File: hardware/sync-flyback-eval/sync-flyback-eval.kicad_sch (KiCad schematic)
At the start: 95 parts, among them J1 RJ45_LED_Shielded, Q1 SiR422DP, Q2 Si7898DP, Q3 MMDT3906, T1 PoE_Transformer, T2 Pulse_Transformer, U1 TPS23754PWPR, U2 TCMT1107

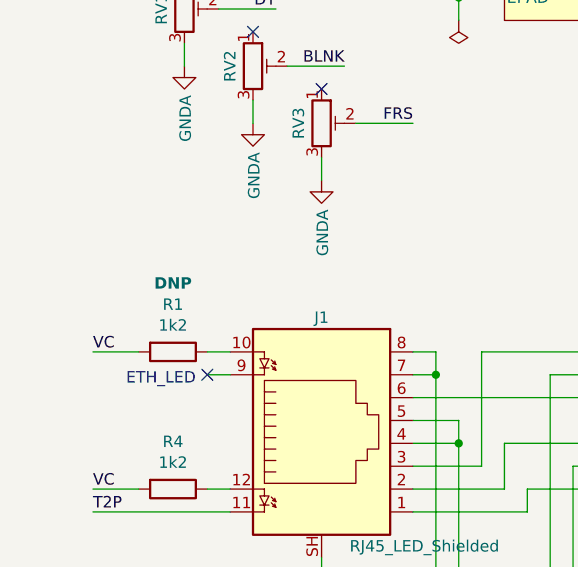
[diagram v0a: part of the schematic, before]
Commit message: flyback: place the current-limiting resistor for the jack
I didn't think I had this spec'd or sourced already.
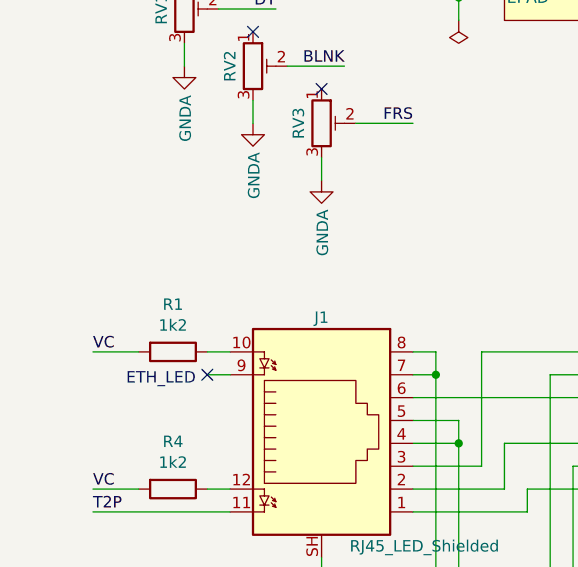
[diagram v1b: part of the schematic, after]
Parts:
- R1: Placement DNP -> (none)
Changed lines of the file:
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@@
       (effects (font (size 1.27 1.27)) hide)
-    )
-    (property "Placement" "DNP" (id 4) (at 29.21 106.68 90)
-      (effects (font (size 1.27 1.27) bold))
     )
     (pin "1")

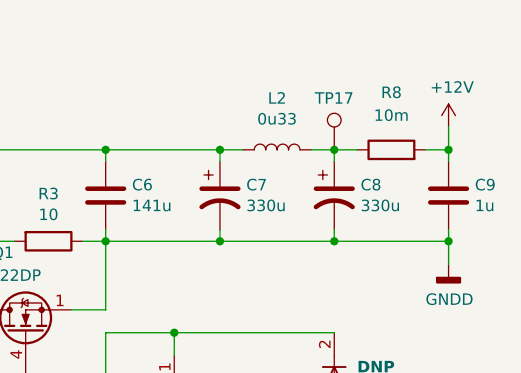
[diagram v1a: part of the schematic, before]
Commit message: flyback: improve testpoints
This changes a number of footprints to be through-hole instead of a
pad. The current sense resistor on the output was also moved to the
outside of the secondary-side output coupling capacitor; plus, an
extra testpoint was added to the other side.
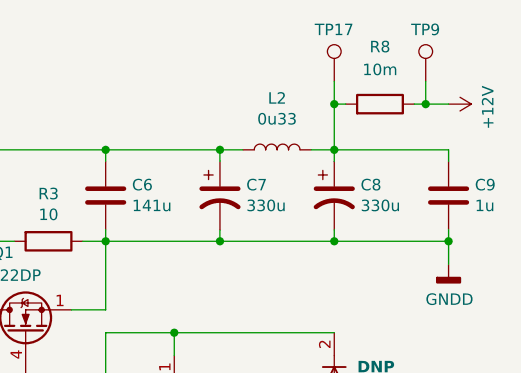
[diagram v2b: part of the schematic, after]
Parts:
- added TP9: VB, TestPoint:TestPoint_Loop_D1.80mm_Drill1.0mm_Beaded, symbol Connector:TestPoint
- TP10, TP11, TP13, TP14, TP15, TP16, TP17, TP2, TP7: footprint TestPoint:TestPoint_Pad_1.5x1.5mm -> TestPoint:TestPoint_Loop_D1.80mm_Drill1.0mm_Beaded
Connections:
- net +12V: now also R8.1, TP9.1; no longer C9.1, R8.2
- net at C8.1, L2.2, TP17.1: now also C9.1, R8.2; no longer R8.1
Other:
- moved on the sheet: R8, TP17

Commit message: flyback: customize a few footprints
These new ones have 3D models.
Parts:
- L1, L2: footprint Inductor_SMD:L_Abracon_ASPI-0630LR -> common:L_Abracon_ASPI-0630LR
- Q1, Q2: footprint Package_SO:PowerPAK_SO-8_Single -> common:PowerPAK_SO-8_Single
- TR1: footprint Transformer_SMD:Transformer_Ethernet_Bourns_PT61017PEL -> common:PT61017PEL
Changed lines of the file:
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@@
     (property "Reference" "L1" (id 0) (at 118.11 18.415 90))
     (property "Value" "3u3" (id 1) (at 118.11 20.7264 90))
-    (property "Footprint" "Inductor_SMD:L_Abracon_ASPI-0630LR" (id 2) (at 118.11 24.13 0)
+    (property "Footprint" "common:L_Abracon_ASPI-0630LR" (id 2) (at 118.11 24.13 0)
       (effects (font (size 1.27 1.27)) hide)
     )
@@
     (property "Reference" "L2" (id 0) (at 242.57 23.495 90))
     (property "Value" "0u33" (id 1) (at 242.57 25.8064 90))
-    (property "Footprint" "Inductor_SMD:L_Abracon_ASPI-0630LR" (id 2) (at 242.57 29.21 0)
+    (property "Footprint" "common:L_Abracon_ASPI-0630LR" (id 2) (at 242.57 29.21 0)
       (effects (font (size 1.27 1.27)) hide)
     )
@@
     (property "Reference" "TR1" (id 0) (at 88.9 135.6868 0))
     (property "Value" "PT61017PEL" (id 1) (at 88.9 133.3754 0))
-    (property "Footprint" "Transformer_SMD:Transformer_Ethernet_Bourns_PT61017PEL" (id 2) (at 88.9 109.22 0)
+    (property "Footprint" "common:PT61017PEL" (id 2) (at 88.9 109.22 0)
       (effects (font (size 1.27 1.27)) hide)
     )
@@
       (effects (font (size 1.27 1.27)) (justify left))
     )
-    (property "Footprint" "Package_SO:PowerPAK_SO-8_Single" (id 2) (at 171.45 66.675 0)
+    (property "Footprint" "common:PowerPAK_SO-8_Single" (id 2) (at 171.45 66.675 0)
       (effects (font (size 1.27 1.27) italic) (justify left) hide)
     )
@@
     (property "Reference" "Q1" (id 0) (at 212.09 40.64 90))
     (property "Value" "SiR422DP" (id 1) (at 212.09 43.18 90))
-    (property "Footprint" "Package_SO:PowerPAK_SO-8_Single" (id 2) (at 216.535 43.18 0)
+    (property "Footprint" "common:PowerPAK_SO-8_Single" (id 2) (at 216.535 43.18 0)
       (effects (font (size 1.27 1.27) italic) (justify left) hide)
     )
@@
     )
     (path "/00000000-0000-0000-0000-00005c1b084a"
-      (reference "L1") (unit 1) (value "3u3") (footprint "Inductor_SMD:L_Abracon_ASPI-0630LR")
+      (reference "L1") (unit 1) (value "3u3") (footprint "common:L_Abracon_ASPI-0630LR")
     )
     (path "/00000000-0000-0000-0000-00005d269ada"
-      (reference "L2") (unit 1) (value "0u33") (footprint "Inductor_SMD:L_Abracon_ASPI-0630LR")
+      (reference "L2") (unit 1) (value "0u33") (footprint "common:L_Abracon_ASPI-0630LR")
     )
     (path "/00000000-0000-0000-0000-00005ef82e6c"
-      (reference "Q1") (unit 1) (value "SiR422DP") (footprint "Package_SO:PowerPAK_SO-8_Single")
+      (reference "Q1") (unit 1) (value "SiR422DP") (footprint "common:PowerPAK_SO-8_Single")
     )
     (path "/00000000-0000-0000-0000-00005ef80cb3"
-      (reference "Q2") (unit 1) (value "Si7898DP") (footprint "Package_SO:PowerPAK_SO-8_Single")
+      (reference "Q2") (unit 1) (value "Si7898DP") (footprint "common:PowerPAK_SO-8_Single")
     )
     (path "/00000000-0000-0000-0000-00005d08d06f"
@@
     )
     (path "/00000000-0000-0000-0000-00005d6ac6f9"
-      (reference "TR1") (unit 1) (value "PT61017PEL") (footprint "Transformer_SMD:Transformer_Ethernet_Bourns_PT61017PEL")
+      (reference "TR1") (unit 1) (value "PT61017PEL") (footprint "common:PT61017PEL")
     )
     (path "/00000000-0000-0000-0000-00005d69703c"

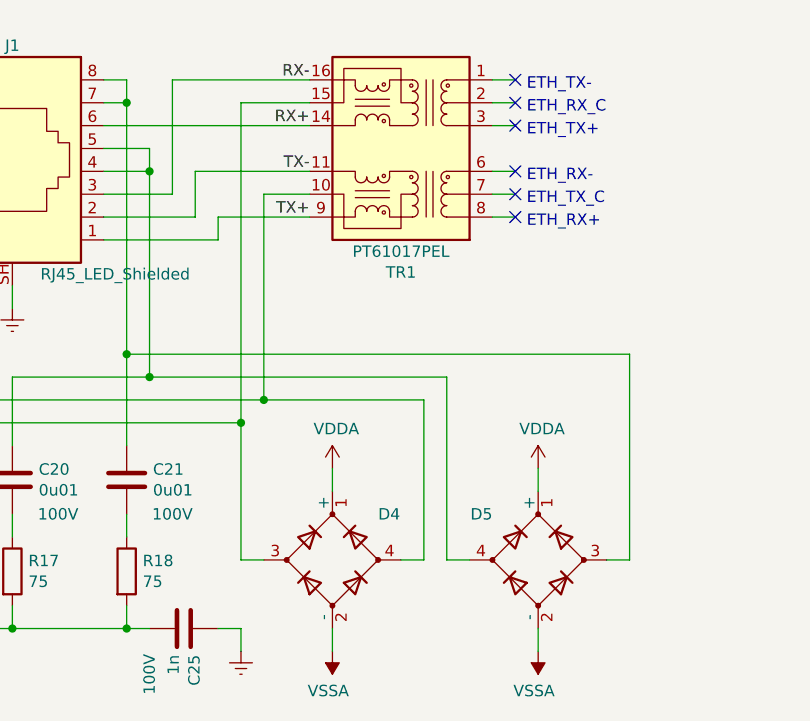
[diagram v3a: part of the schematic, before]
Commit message: flyback: shuffle a few connections to make layout easier
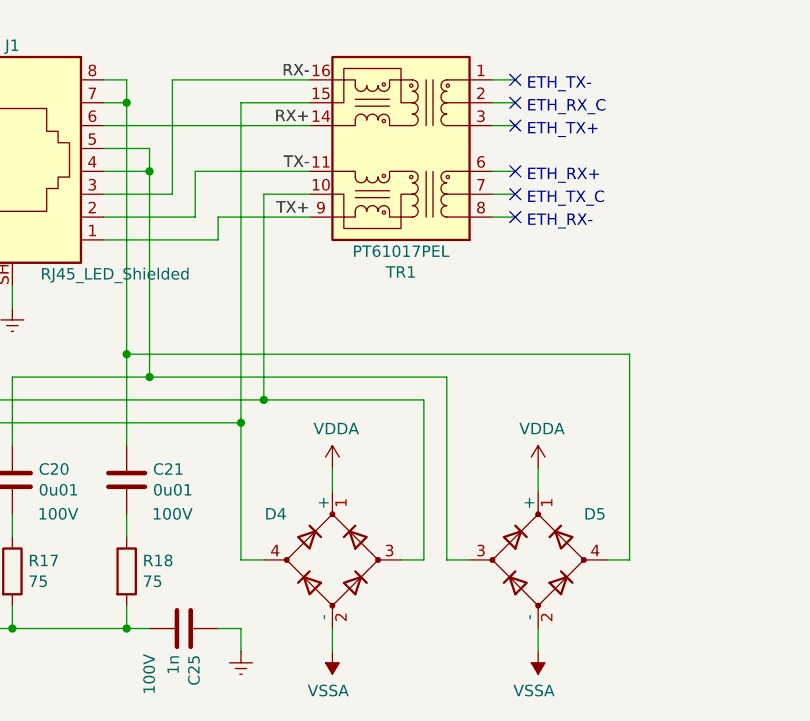
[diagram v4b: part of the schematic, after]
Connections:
- net at C20.1, J1.4, J1.5: now also D5.3; no longer D5.4
- net at C21.1, J1.7, J1.8: now also D5.4; no longer D5.3
- net at C18.1, TR1.15 (C_TX): now also D4.4; no longer D4.3
- net at C19.1, TR1.10 (C_RX): now also D4.3; no longer D4.4
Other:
- moved on the sheet: D4, D5
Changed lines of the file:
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@@
-    (stroke (width 0) (type default) (color 0 0 0 0))
-  )
-  (wire (pts (xy 68.58 132.08) (xy 68.58 129.54))
     (stroke (width 0) (type default) (color 0 0 0 0))
   )
@@
     (stroke (width 0) (type default) (color 0 0 0 0))
   )
-  (wire (pts (xy 66.04 124.46) (xy 78.74 124.46))
-    (stroke (width 0) (type default) (color 0 0 0 0))
-  )
   (wire (pts (xy 177.8 72.39) (xy 180.34 72.39))
     (stroke (width 0) (type default) (color 0 0 0 0))
@@
     (stroke (width 0) (type default) (color 0 0 0 0))
   )
+  (wire (pts (xy 68.58 129.54) (xy 78.74 129.54))
+    (stroke (width 0) (type default) (color 0 0 0 0))
+  )
   (wire (pts (xy 154.94 24.13) (xy 177.8 24.13))
     (stroke (width 0) (type default) (color 0 0 0 0))
@@
     (stroke (width 0) (type default) (color 0 0 0 0))
   )
+  (wire (pts (xy 55.88 129.54) (xy 66.04 129.54))
+    (stroke (width 0) (type default) (color 0 0 0 0))
+  )
   (wire (pts (xy 215.9 72.39) (xy 215.9 73.66))
     (stroke (width 0) (type default) (color 0 0 0 0))
@@
   )
   (wire (pts (xy 165.1 36.83) (xy 167.64 36.83))
-    (stroke (width 0) (type default) (color 0 0 0 0))
-  )
-  (wire (pts (xy 68.58 129.54) (xy 78.74 129.54))
     (stroke (width 0) (type default) (color 0 0 0 0))
   )
@@
     (stroke (width 0) (type default) (color 0 0 0 0))
   )
-  (wire (pts (xy 55.88 129.54) (xy 66.04 129.54))
+  (wire (pts (xy 66.04 124.46) (xy 78.74 124.46))
     (stroke (width 0) (type default) (color 0 0 0 0))
   )
@@
     (stroke (width 0) (type default) (color 0 0 0 0))
   )
+  (wire (pts (xy 68.58 132.08) (xy 68.58 129.54))
+    (stroke (width 0) (type default) (color 0 0 0 0))
+  )
   (wire (pts (xy 93.98 49.53) (xy 109.22 49.53))
     (stroke (width 0) (type default) (color 0 0 0 0))
@@
     (stroke (width 0) (type default) (color 0 0 0 0))
   )
-  (wire (pts (xy 66.04 129.54) (xy 66.04 124.46))
-    (stroke (width 0) (type default) (color 0 0 0 0))
-  )
   (wire (pts (xy 58.42 114.3) (xy 55.88 114.3))
     (stroke (width 0) (type default) (color 0 0 0 0))
@@
   )
   (wire (pts (xy 238.76 29.21) (xy 236.22 29.21))
+    (stroke (width 0) (type default) (color 0 0 0 0))
+  )
+  (wire (pts (xy 66.04 124.46) (xy 66.04 129.54))
     (stroke (width 0) (type default) (color 0 0 0 0))
   )
@@
     (effects (font (size 1.27 1.27)) (justify left bottom))
   )
-  (text "ETH_RX-" (at 102.87 125.73 0)
-    (effects (font (size 1.27 1.27)) (justify left bottom))
-  )
-  (text "ETH_RX+" (at 102.87 130.81 0)
+  (text "ETH_RX-" (at 102.87 130.81 0)
+    (effects (font (size 1.27 1.27)) (justify left bottom))
+  )
+  (text "ETH_RX+" (at 102.87 125.73 0)
     (effects (font (size 1.27 1.27)) (justify left bottom))
   )
@@
     (pin "2")
   )
-  (symbol (lib_id "Device:D_Bridge_+-AA") (at 81.28 167.64 90) (unit 1)
-    (in_bom yes) (on_board yes)
-    (property "Reference" "D4" (id 0) (at 86.36 162.56 90)
+  (symbol (lib_id "Device:D_Bridge_+-AA") (at 81.28 167.64 270) (mirror x) (unit 1)
+    (in_bom yes) (on_board yes)
+    (property "Reference" "D4" (id 0) (at 76.2 162.56 90)
       (effects (font (size 1.27 1.27)) (justify right))
     )
-    (property "Value" "D_Bridge_+-AA" (id 1) (at 89.9414 168.783 90)
+    (property "Value" "D_Bridge_+-AA" (id 1) (at 72.6186 168.783 90)
       (effects (font (size 1.27 1.27)) (justify right) hide)
     )
@@
     (pin "4")
   )
-  (symbol (lib_id "Device:D_Bridge_+-AA") (at 104.14 167.64 270) (mirror x) (unit 1)
-    (in_bom yes) (on_board yes)
-    (property "Reference" "D5" (id 0) (at 99.06 162.56 90)
+  (symbol (lib_id "Device:D_Bridge_+-AA") (at 104.14 167.64 90) (unit 1)
+    (in_bom yes) (on_board yes)
+    (property "Reference" "D5" (id 0) (at 109.22 162.56 90)
       (effects (font (size 1.27 1.27)) (justify right))
     )
-    (property "Value" "D_Bridge_+-AA" (id 1) (at 95.4786 168.783 90)
+    (property "Value" "D_Bridge_+-AA" (id 1) (at 112.8014 168.783 90)
       (effects (font (size 1.27 1.27)) (justify right) hide)
     )

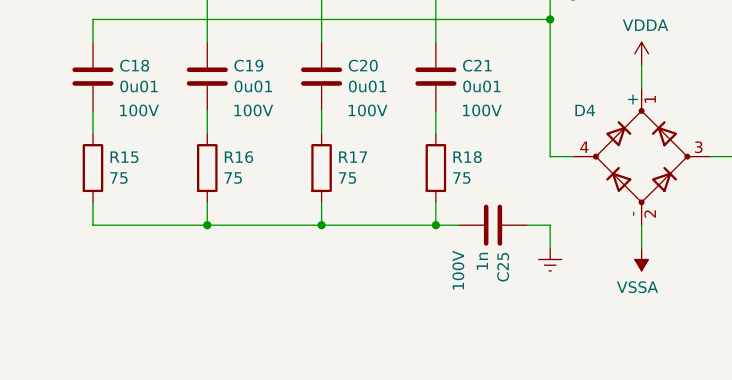
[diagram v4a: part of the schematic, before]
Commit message: flyback: add second earth-coupling capacitor to simplify pcb layout
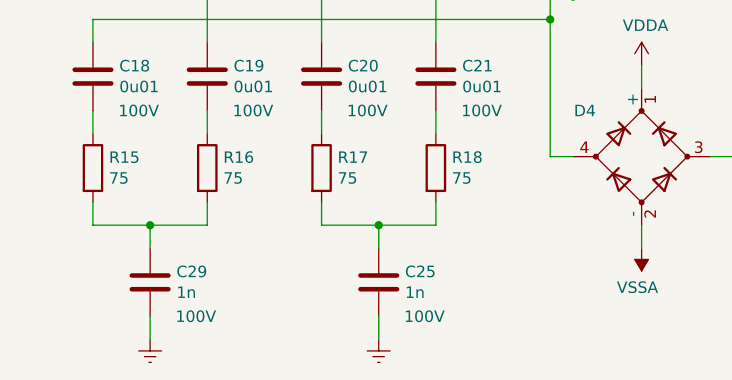
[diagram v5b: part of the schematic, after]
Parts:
- added C29: 1n, Capacitor_SMD:C_0402_1005Metric, symbol Device:C
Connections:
- net Earth: now also C25.2, C29.2; no longer C25.1
- new net: C29.1, R15.2, R16.2
- new net: C25.1, R17.2, R18.2
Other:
- moved on the sheet: C25
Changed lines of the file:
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@@
   (junction (at 111.76 24.13) (diameter 0) (color 0 0 0 0)
   )
-  (junction (at 58.42 175.26) (diameter 0) (color 0 0 0 0)
-  )
   (junction (at 200.66 39.37) (diameter 0) (color 0 0 0 0)
   )
@@
   (junction (at 210.82 107.95) (diameter 0) (color 0 0 0 0)
   )
+  (junction (at 26.67 175.26) (diameter 0) (color 0 0 0 0)
+  )
   (junction (at 60.96 74.93) (diameter 0) (color 0 0 0 0)
   )
@@
   (junction (at 58.42 144.78) (diameter 0) (color 0 0 0 0)
   )
-  (junction (at 45.72 175.26) (diameter 0) (color 0 0 0 0)
-  )
-  (junction (at 33.02 175.26) (diameter 0) (color 0 0 0 0)
-  )
   (junction (at 25.4 41.91) (diameter 0) (color 0 0 0 0)
   )
@@
   (junction (at 200.66 107.95) (diameter 0) (color 0 0 0 0)
   )
+  (junction (at 52.07 175.26) (diameter 0) (color 0 0 0 0)
+  )
   (junction (at 60.96 147.32) (diameter 0) (color 0 0 0 0)
   )
@@
     (stroke (width 0) (type default) (color 0 0 0 0))
   )
+  (wire (pts (xy 26.67 175.26) (xy 33.02 175.26))
+    (stroke (width 0) (type default) (color 0 0 0 0))
+  )
   (wire (pts (xy 88.9 167.64) (xy 91.44 167.64))
     (stroke (width 0) (type default) (color 0 0 0 0))
@@
     (stroke (width 0) (type default) (color 0 0 0 0))
   )
+  (wire (pts (xy 52.07 175.26) (xy 58.42 175.26))
+    (stroke (width 0) (type default) (color 0 0 0 0))
+  )
   (wire (pts (xy 149.86 57.15) (xy 148.59 57.15))
     (stroke (width 0) (type default) (color 0 0 0 0))
@@
     (stroke (width 0) (type default) (color 0 0 0 0))
   )
-  (wire (pts (xy 20.32 175.26) (xy 33.02 175.26))
+  (wire (pts (xy 20.32 175.26) (xy 26.67 175.26))
     (stroke (width 0) (type default) (color 0 0 0 0))
   )
@@
     (stroke (width 0) (type default) (color 0 0 0 0))
   )
-  (wire (pts (xy 71.12 175.26) (xy 71.12 177.8))
-    (stroke (width 0) (type default) (color 0 0 0 0))
-  )
   (wire (pts (xy 223.52 29.21) (xy 236.22 29.21))
     (stroke (width 0) (type default) (color 0 0 0 0))
@@
     (stroke (width 0) (type default) (color 0 0 0 0))
   )
+  (wire (pts (xy 52.07 185.42) (xy 52.07 187.96))
+    (stroke (width 0) (type default) (color 0 0 0 0))
+  )
   (wire (pts (xy 104.14 177.8) (xy 104.14 175.26))
     (stroke (width 0) (type default) (color 0 0 0 0))
@@
     (stroke (width 0) (type default) (color 0 0 0 0))
   )
+  (wire (pts (xy 26.67 185.42) (xy 26.67 187.96))
+    (stroke (width 0) (type default) (color 0 0 0 0))
+  )
   (wire (pts (xy 190.5 107.95) (xy 190.5 115.57))
     (stroke (width 0) (type default) (color 0 0 0 0))
@@
     (stroke (width 0) (type default) (color 0 0 0 0))
   )
-  (wire (pts (xy 58.42 175.26) (xy 60.96 175.26))
-    (stroke (width 0) (type default) (color 0 0 0 0))
-  )
   (wire (pts (xy 109.22 77.47) (xy 111.76 77.47))
     (stroke (width 0) (type default) (color 0 0 0 0))
@@
     (stroke (width 0) (type default) (color 0 0 0 0))
   )
-  (wire (pts (xy 33.02 175.26) (xy 45.72 175.26))
+  (wire (pts (xy 52.07 175.26) (xy 52.07 177.8))
     (stroke (width 0) (type default) (color 0 0 0 0))
   )
-  (wire (pts (xy 45.72 175.26) (xy 58.42 175.26))
+  (wire (pts (xy 45.72 175.26) (xy 52.07 175.26))
     (stroke (width 0) (type default) (color 0 0 0 0))
   )
@@
     (stroke (width 0) (type default) (color 0 0 0 0))
   )
-  (wire (pts (xy 68.58 175.26) (xy 71.12 175.26))
-    (stroke (width 0) (type default) (color 0 0 0 0))
-  )
   (wire (pts (xy 259.08 24.13) (xy 261.62 24.13))
     (stroke (width 0) (type default) (color 0 0 0 0))
@@
     (stroke (width 0) (type default) (color 0 0 0 0))
   )
+  (wire (pts (xy 26.67 175.26) (xy 26.67 177.8))
+    (stroke (width 0) (type default) (color 0 0 0 0))
+  )
   (wire (pts (xy 34.29 41.91) (xy 38.1 41.91))
     (stroke (width 0) (type default) (color 0 0 0 0))
@@
     (pin "2")
   )
-  (symbol (lib_id "Device:C") (at 64.77 175.26 270) (unit 1)
+  (symbol (lib_id "Device:C") (at 52.07 181.61 0) (unit 1)
     (in_bom yes) (on_board yes)
-    (property "Reference" "C25" (id 0) (at 65.9384 178.181 0)
+    (property "Reference" "C25" (id 0) (at 54.991 180.4416 0)
       (effects (font (size 1.27 1.27)) (justify left))
     )
-    (property "Value" "1n" (id 1) (at 63.627 178.181 0)
+    (property "Value" "1n" (id 1) (at 54.991 182.753 0)
       (effects (font (size 1.27 1.27)) (justify left))
     )
-    (property "Footprint" "Capacitor_SMD:C_0402_1005Metric" (id 2) (at 60.96 176.2252 0)
+    (property "Footprint" "Capacitor_SMD:C_0402_1005Metric" (id 2) (at 53.0352 185.42 0)
       (effects (font (size 1.27 1.27)) hide)
     )
-    (property "Datasheet" "~" (id 3) (at 64.77 175.26 0)
+    (property "Datasheet" "~" (id 3) (at 52.07 181.61 0)
       (effects (font (size 1.27 1.27)) hide)
     )
-    (property "Voltage" "100V" (id 4) (at 60.96 180.34 0))
+    (property "Voltage" "100V" (id 4) (at 57.15 185.42 0))
     (pin "1")
     (pin "2")
   )
-  (symbol (lib_id "power:Earth") (at 71.12 177.8 0) (unit 1)
+  (symbol (lib_id "power:Earth") (at 52.07 187.96 0) (unit 1)
     (in_bom yes) (on_board yes)
-    (property "Reference" "#PWR027" (id 0) (at 71.12 184.15 0)
+    (property "Reference" "#PWR027" (id 0) (at 52.07 194.31 0)
       (effects (font (size 1.27 1.27)) hide)
     )
-    (property "Value" "Earth" (id 1) (at 71.12 181.61 0)
+    (property "Value" "Earth" (id 1) (at 52.07 191.77 0)
       (effects (font (size 1.27 1.27)) hide)
     )
-    (property "Footprint" "" (id 2) (at 71.12 177.8 0)
+    (property "Footprint" "" (id 2) (at 52.07 187.96 0)
       (effects (font (size 1.27 1.27)) hide)
     )
-    (property "Datasheet" "~" (id 3) (at 71.12 177.8 0)
+    (property "Datasheet" "~" (id 3) (at 52.07 187.96 0)
       (effects (font (size 1.27 1.27)) hide)
     )
@@
     (pin "2")
   )
+  (symbol (lib_id "Device:C") (at 26.67 181.61 0) (unit 1)
+    (in_bom yes) (on_board yes)
+    (property "Reference" "C29" (id 0) (at 29.591 180.4416 0)
+      (effects (font (size 1.27 1.27)) (justify left))
+    )
+    (property "Value" "1n" (id 1) (at 29.591 182.753 0)
+      (effects (font (size 1.27 1.27)) (justify left))
+    )
+    (property "Footprint" "Capacitor_SMD:C_0402_1005Metric" (id 2) (at 27.6352 185.42 0)
+      (effects (font (size 1.27 1.27)) hide)
+    )
+    (property "Datasheet" "~" (id 3) (at 26.67 181.61 0)
+      (effects (font (size 1.27 1.27)) hide)
+    )
+    (property "Voltage" "100V" (id 4) (at 31.75 185.42 0))
+    (pin "1")
+    (pin "2")
+  )
   (symbol (lib_id "Connector:TestPoint") (at 170.18 139.7 0) (unit 1)
     (in_bom yes) (on_board yes)
@@
     (pin "1")
   )
+  (symbol (lib_id "power:Earth") (at 26.67 187.96 0) (unit 1)
+    (in_bom yes) (on_board yes)
+    (property "Reference" "#PWR036" (id 0) (at 26.67 194.31 0)
+      (effects (font (size 1.27 1.27)) hide)
+    )
+    (property "Value" "Earth" (id 1) (at 26.67 191.77 0)
+      (effects (font (size 1.27 1.27)) hide)
+    )
+    (property "Footprint" "" (id 2) (at 26.67 187.96 0)
+      (effects (font (size 1.27 1.27)) hide)
+    )
+    (property "Datasheet" "~" (id 3) (at 26.67 187.96 0)
+      (effects (font (size 1.27 1.27)) hide)
+    )
+    (pin "1")
+  )
   (symbol (lib_id "power:GNDA") (at 45.72 95.25 0) (unit 1)
     (in_bom yes) (on_board yes)
@@
       (reference "#PWR035") (unit 1) (value "GNDA") (footprint "")
     )
+    (path "/abd4dc08-6261-40f3-a11d-4fcc253c402a"
+      (reference "#PWR036") (unit 1) (value "Earth") (footprint "")
+    )
     (path "/00000000-0000-0000-0000-00005cbb7e41"
       (reference "#PWR043") (unit 1) (value "VDDA") (footprint "")
@@
       (reference "C28") (unit 1) (value "6n8") (footprint "Capacitor_SMD:C_0402_1005Metric")
     )
+    (path "/9d251859-fbb8-4f24-860a-10bcae161ec6"
+      (reference "C29") (unit 1) (value "1n") (footprint "Capacitor_SMD:C_0402_1005Metric")
+    )
     (path "/00000000-0000-0000-0000-00005c1cc06c"
